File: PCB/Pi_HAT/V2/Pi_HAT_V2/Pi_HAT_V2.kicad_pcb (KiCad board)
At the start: 2 copper layers, 59 x 69.6 mm, 18 parts, among them J1 MPU9250, J2 Pi GPIO, J3 Display, J4 Solenoid I2C, J5 XT60PW-M

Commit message: Still more to do
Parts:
- removed VR1, VR2, VR3: LM78M05CDTX/NOPB, .pretty:VREG_L7805ACD2T
- added C1: 22u, Capacitor_SMD:C_1210_3225Metric_Pad1.33x2.70mm_HandSolder, F.Cu at (65.8, 88.9)
- added C2: 22u, Capacitor_SMD:C_1210_3225Metric_Pad1.33x2.70mm_HandSolder, F.Cu at (65.8, 93.2)
- added C3: 100n, Capacitor_SMD:C_0805_2012Metric_Pad1.18x1.45mm_HandSolder, F.Cu at (59.4, 97.3)
- added C4: 100n, Capacitor_SMD:C_0805_2012Metric_Pad1.18x1.45mm_HandSolder, F.Cu at (54.6, 97.3)
- added C5: 22u, Capacitor_SMD:C_1210_3225Metric_Pad1.33x2.70mm_HandSolder, F.Cu at (71.9, 86.8)
- added C6: 22u, Capacitor_SMD:C_1210_3225Metric_Pad1.33x2.70mm_HandSolder, F.Cu at (72.7, 82.5)
- added C7: 22u, Capacitor_SMD:C_1210_3225Metric_Pad1.33x2.70mm_HandSolder, F.Cu at (66.7, 82.5)
- added L1: 4.7u, .pretty:744777004, F.Cu at (56.9, 91.3)
- added R1: 75K, Resistor_SMD:R_0805_2012Metric_Pad1.20x1.40mm_HandSolder, F.Cu at (65.2, 96.8)
- added R2: 180K, Resistor_SMD:R_1206_3216Metric_Pad1.30x1.75mm_HandSolder, F.Cu at (78.7, 82.0)
- added R3: 20, Resistor_SMD:R_0805_2012Metric_Pad1.20x1.40mm_HandSolder, F.Cu at (77.1, 90.4)
- added R4: 20, Resistor_SMD:R_0805_2012Metric_Pad1.20x1.40mm_HandSolder, F.Cu at (78.1, 85.2)
- added R5: 7.5K, Resistor_SMD:R_0805_2012Metric_Pad1.20x1.40mm_HandSolder, F.Cu at (71.2, 94.8)
- added RV1: 200K, .pretty:TRIM_3296W-1-204LF, F.Cu at (58.1, 83.6)
- added U1: MP2315GJ-Z, .pretty:SOT65P280X100-8N, F.Cu at (72.1, 91.1)
- C1: value C -> 22u; footprint Capacitor_THT:C_Rect_L7.0mm_W2.5mm_P5.00mm -> Capacitor_SMD:C_1210_3225Metric_Pad1.33x2.70mm_HandSolder
- C2: value C_Polarized -> 22u; footprint Capacitor_THT:CP_Radial_D4.0mm_P1.50mm -> Capacitor_SMD:C_1210_3225Metric_Pad1.33x2.70mm_HandSolder
- G***: moved to B.Cu
- J2: value Pi GPIO -> Pi_GPIO
- TB1: value ARDUINO NANO -> ARDUINO_NANO
- moved C2 34.7 mm to (76.2, 103.1)
- moved G*** 30.4 mm to (118.3, 114.8), turned to -90 degrees
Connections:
- C2 pad 1: /5V -> 12V
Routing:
- net /5V: track 125.2 -> 14.1 mm
- net 12V: track 99.9 -> 34.4 mm
- net GND: track 88.5 -> 36.8 mm, vias 6 -> 2
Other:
- board text added: "PI HAT 08/22/22 EASY CONTROLS Designed by: Jacob Romeo"
- board text removed: "PI HAT EASY CONTROLS Designed by: Jacob Romeo"

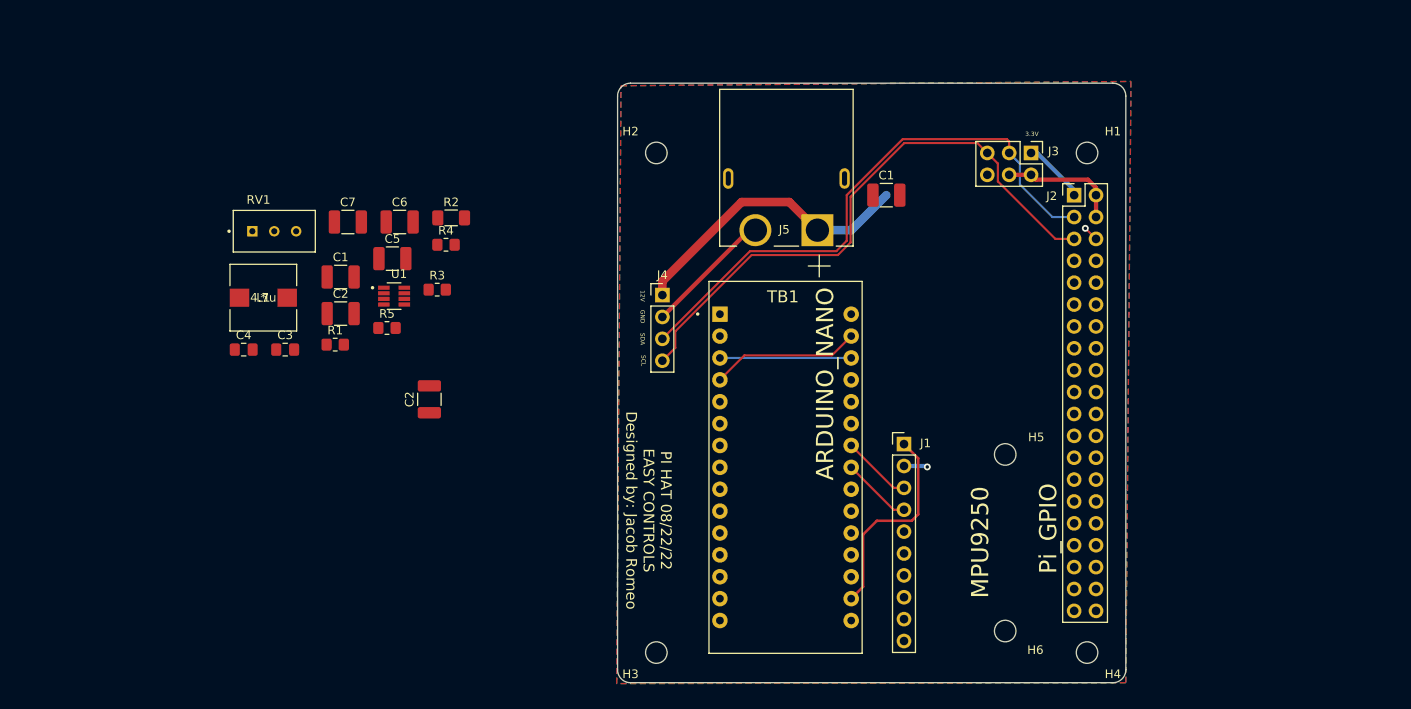
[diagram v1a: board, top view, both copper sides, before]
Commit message: Finished Buch .sch
Next need to start/finish the PCB traces
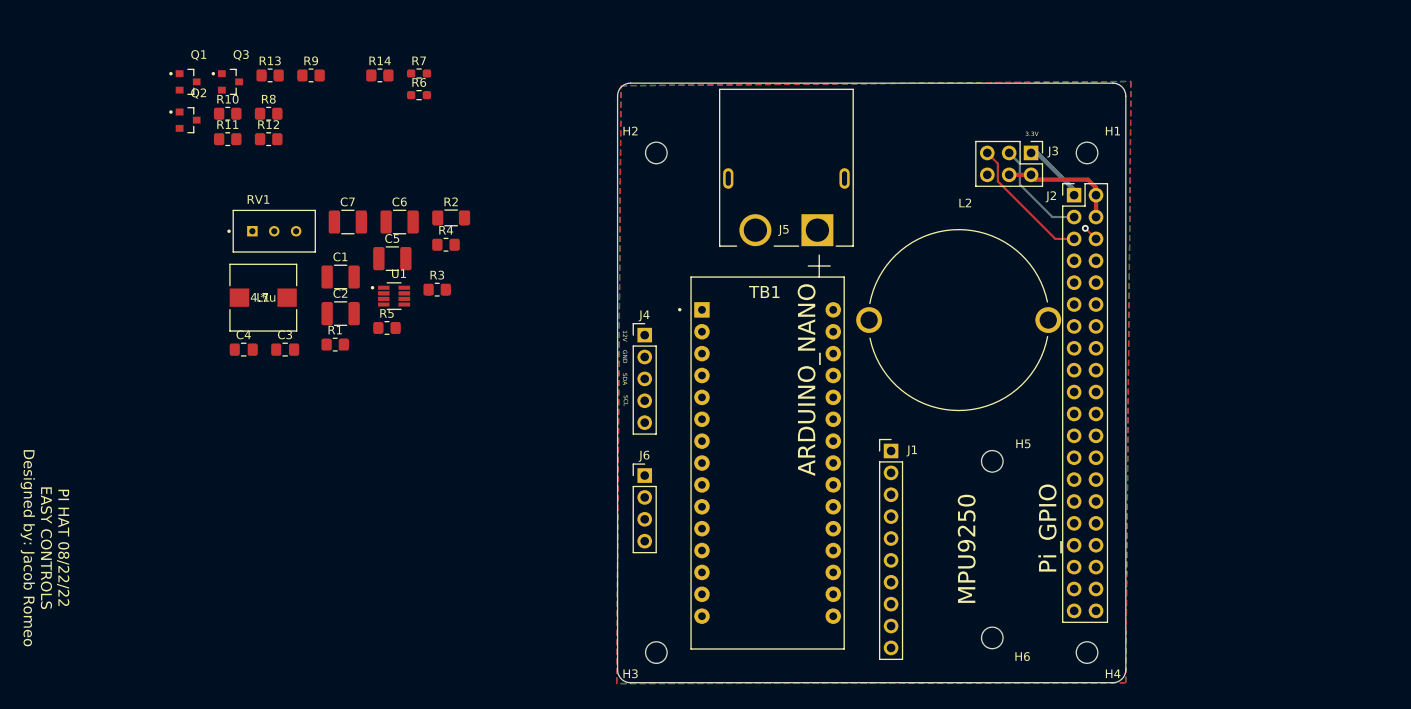
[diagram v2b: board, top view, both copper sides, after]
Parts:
- removed the C1 at (129.2, 79.4)
- removed the C2 at (76.2, 103.1)
- removed G***: LOGO, .pretty:eppl_logo
- added J6: Conn_01x04_Male, Connector_PinHeader_2.54mm:PinHeader_1x04_P2.54mm_Vertical, F.Cu at (101.2, 112.0)
- added L2: 220u, .pretty:IND_AIRD-02-151K, F.Cu at (137.6, 93.9)
- added Q1: BSS138_RFG, .pretty:TRANS_BSS138_RFG, F.Cu at (48.1, 66.2)
- added Q2: BSS138_RFG, .pretty:TRANS_BSS138_RFG, F.Cu at (48.1, 70.7)
- added Q3: BSS138_RFG, .pretty:TRANS_BSS138_RFG, F.Cu at (53.1, 66.2)
- added R10: 10K, Resistor_SMD:R_0805_2012Metric_Pad1.20x1.40mm_HandSolder, F.Cu at (52.7, 70.0)
- added R11: 10K, Resistor_SMD:R_0805_2012Metric_Pad1.20x1.40mm_HandSolder, F.Cu at (52.7, 72.9)
- added R12: 10K, Resistor_SMD:R_0805_2012Metric_Pad1.20x1.40mm_HandSolder, F.Cu at (57.5, 72.9)
- added R13: 10K, Resistor_SMD:R_0805_2012Metric_Pad1.20x1.40mm_HandSolder, F.Cu at (57.7, 65.5)
- added R14: 10K, Resistor_SMD:R_0805_2012Metric_Pad1.20x1.40mm_HandSolder, F.Cu at (70.4, 65.5)
- added R6: 700, Resistor_SMD:R_0603_1608Metric_Pad0.98x0.95mm_HandSolder, F.Cu at (75.0, 67.8)
- added R7: 700, Resistor_SMD:R_0603_1608Metric_Pad0.98x0.95mm_HandSolder, F.Cu at (75.0, 65.3)
- added R8: 10K, Resistor_SMD:R_0805_2012Metric_Pad1.20x1.40mm_HandSolder, F.Cu at (57.5, 70.0)
- added R9: 10K, Resistor_SMD:R_0805_2012Metric_Pad1.20x1.40mm_HandSolder, F.Cu at (62.4, 65.5)
- J4: value Solenoid I2C -> Conn_01x05_Male; footprint Connector_PinHeader_2.54mm:PinHeader_1x04_P2.54mm_Vertical -> Connector_PinHeader_2.54mm:PinHeader_1x05_P2.54mm_Vertical
- moved J4 5.08 mm to (101.2, 95.7)
- moved TB1 2.14 mm to (115.4, 110.5)
- moved H6 1.70 mm to (141.5, 130.8)
- moved H5 1.70 mm to (141.5, 110.3)
- moved J1 1.70 mm to (129.8, 109.1)
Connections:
- J2 pad 10: unconnected-(J2-Pad10) -> /RXP
- J2 pad 8: unconnected-(J2-Pad8) -> /TXP
- J4 pad 3: /SDA -> /SCL
- J4 pad 4: /SCL -> /SDA
- R2 pad 1: unconnected-(R2-Pad1) -> /Buck Converter/SYNC
- TB1 pad 1: unconnected-(TB1-Pad1) -> /TXN
- TB1 pad 2: unconnected-(TB1-Pad2) -> /RXN
- TB1 pad 27: unconnected-(TB1-Pad27) -> /5VN
- TB1 pad 28: unconnected-(TB1-Pad28) -> Net-(R14-Pad2)
- TB1 pad 3: unconnected-(TB1-Pad28) -> Net-(R14-Pad2)
- TB1 pad 30: unconnected-(TB1-Pad30) -> /5V
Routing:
- net /SDA: track 66.4 -> 12.0 mm
- net /SCL: track 68.3 -> 15.4 mm
- net GND: track 36.8 -> 1.75 mm, vias 2 -> 1
- net 12V: track 34.4 -> 0.00 mm
- net 3.3VN: track 24.2 -> 0.00 mm
- net unconnected-(TB1-Pad28): track 15.2 -> 0.00 mm
- net SDAN: track 8.17 -> 0.00 mm
- net SCLN: track 8.17 -> 0.00 mm

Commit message: Updated
Added NANO_HAT and finished the PI_HAT V2 .sch, need to start/finish traces
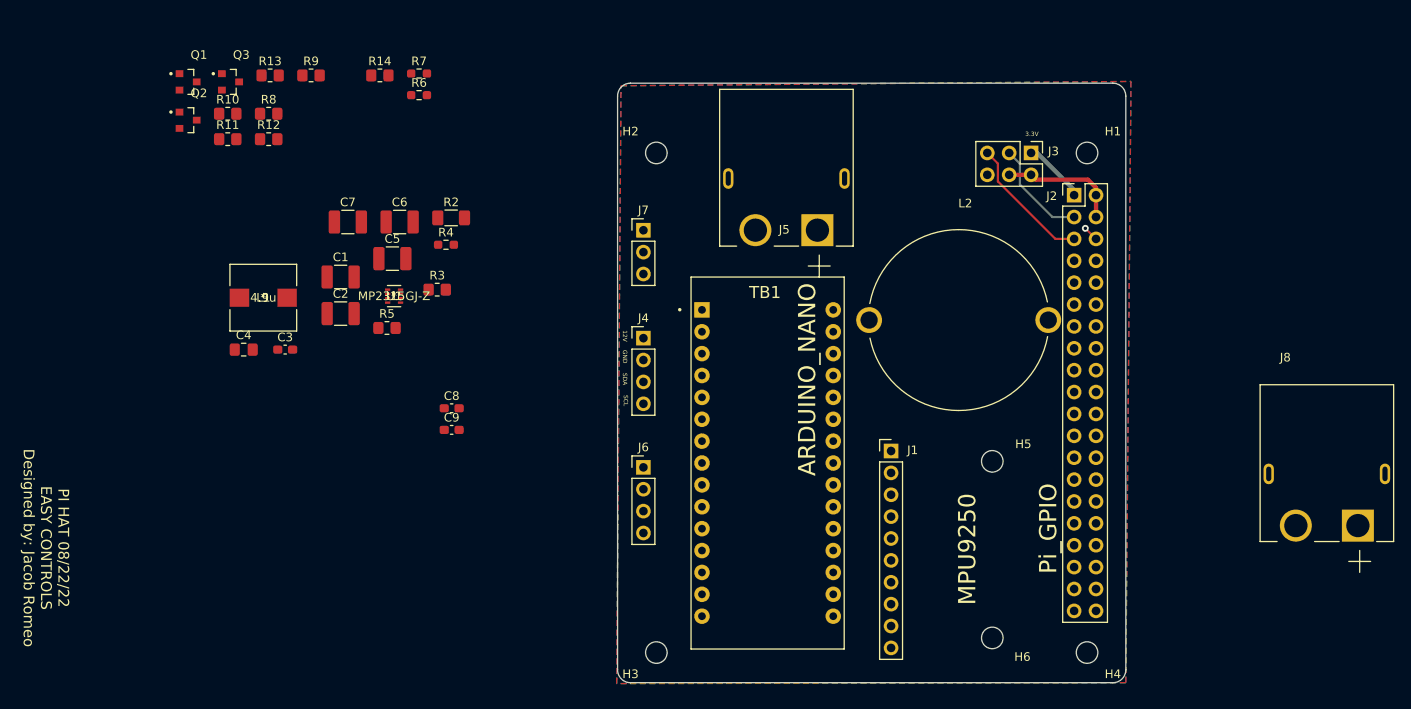
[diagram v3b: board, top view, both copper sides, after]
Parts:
- removed R1: 75K, Resistor_SMD:R_0805_2012Metric_Pad1.20x1.40mm_HandSolder
- removed RV1: 200K, .pretty:TRIM_3296W-1-204LF
- added C8: 6.8n, Capacitor_SMD:C_0603_1608Metric_Pad1.08x0.95mm_HandSolder, F.Cu at (78.7, 104.1)
- added C9: 10p, Capacitor_SMD:C_0603_1608Metric_Pad1.08x0.95mm_HandSolder, F.Cu at (78.7, 106.7)
- added J7: Pressure Sensor, Connector_PinHeader_2.54mm:PinHeader_1x03_P2.54mm_Vertical, F.Cu at (101.0, 83.5)
- added J8: XT60PW-M, .pretty:AMASS_XT60PW-M, F.Cu at (180.3, 111.8)
- C2: value 22u -> 0.1u
- C3: value 100n -> 1n; footprint Capacitor_SMD:C_0805_2012Metric_Pad1.18x1.45mm_HandSolder -> Capacitor_SMD:C_0603_1608Metric_Pad1.08x0.95mm_HandSolder
- C4: value 100n -> 1u
- J4: value Conn_01x05_Male -> Conn_01x04_Male; footprint Connector_PinHeader_2.54mm:PinHeader_1x05_P2.54mm_Vertical -> Connector_PinHeader_2.54mm:PinHeader_1x04_P2.54mm_Vertical
- L1: value 4.7u -> 4.9u
- R14: value 10K -> 40.2k
- R2: value 180K -> 604k
- R3: value 20 -> 15k
- R4: footprint Resistor_SMD:R_0805_2012Metric_Pad1.20x1.40mm_HandSolder -> Resistor_SMD:R_0603_1608Metric_Pad0.98x0.95mm_HandSolder
- R5: value 7.5K -> 7.68K
- U1: footprint .pretty:SOT65P280X100-8N -> .pretty:MP2393GTL-P
- moved J6 0.96 mm to (101.0, 111.0)
- moved J4 0.38 mm to (101.0, 96.0)
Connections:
- R14 pad 1: GND -> Net-(C5-Pad1)
- R14 pad 2: Net-(R14-Pad2) -> Net-(C9-Pad2)
- R2 pad 1: /Buck Converter/SYNC -> 12V
- R3 pad 2: Net-(R3-Pad2) -> Net-(C9-Pad2)
- R5 pad 2: Net-(R3-Pad2) -> Net-(C9-Pad2)
- R6 pad 1: GND -> /SDA
- R6 pad 2: /SDA -> 3.3VP
- R7 pad 1: GND -> /SCL
- R7 pad 2: /SCL -> 3.3VP
- TB1 pad 19: unconnected-(TB1-Pad19) -> /PS
- TB1 pad 28: Net-(R14-Pad2) -> unconnected-(TB1-Pad28)
- TB1 pad 3: Net-(R14-Pad2) -> unconnected-(TB1-Pad28)
- U1 pad 1: Net-(R1-Pad2) -> Net-(C3-Pad1)
- U1 pad 7: Net-(C3-Pad1) -> Net-(C8-Pad1)

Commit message: Updated (Gerber)
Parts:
- removed J8: XT60PW-M, .pretty:AMASS_XT60PW-M
- C1, C2, C3, C4, C5, C6, C7, C8, C9, L1, Q1, Q2, Q3, R10, R11, R12, R13, R14, R2, R3, R4, R5, R6, R7, R8, R9, U1: moved to B.Cu
- moved L1 92.7 mm to (146.5, 67.7)
- moved C4 89.0 mm to (140.2, 73.1), turned to 180 degrees
- moved C3 85.4 mm to (140.2, 69.5), turned to -90 degrees
- moved R7 75.3 mm to (147.8, 84.5), turned to 90 degrees
- moved R6 74.0 mm to (147.8, 80.7), turned to 90 degrees
- moved R5 73.8 mm to (139.2, 66.1), turned to 180 degrees
- moved Q1 70.3 mm to (108.2, 102.7), turned to 90 degrees
- moved C7 70.0 mm to (135.6, 94.9), turned to 180 degrees
- moved Q2 69.5 mm to (113.9, 93.0), turned to -90 degrees
- moved C9 69.4 mm to (135.0, 66.1)
- moved U1 68.7 mm to (137.2, 69.5), turned to 180 degrees
- moved C1 68.0 mm to (132.4, 74.6), turned to 90 degrees
- moved R3 67.7 mm to (139.3, 63.8), turned to 180 degrees
- moved R11 65.4 mm to (113.9, 96.1), turned to 180 degrees
- moved C8 65.0 mm to (133.8, 69.5), turned to -90 degrees
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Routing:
- net /SCL: track 15.4 -> 0.00 mm
- net /SDA: track 12.0 -> 0.00 mm
- net /5V: track 14.1 -> 2.54 mm
- net 3.3VP: track 7.38 -> 0.00 mm
- net GND: track 1.75 -> 0.00 mm, vias 1 -> 0
- removed copper zone on B.Cu, net GND
- removed copper zone on F.Cu, net GND
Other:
- board size 59 x 69.6 mm -> 71.7 x 75.3 mm

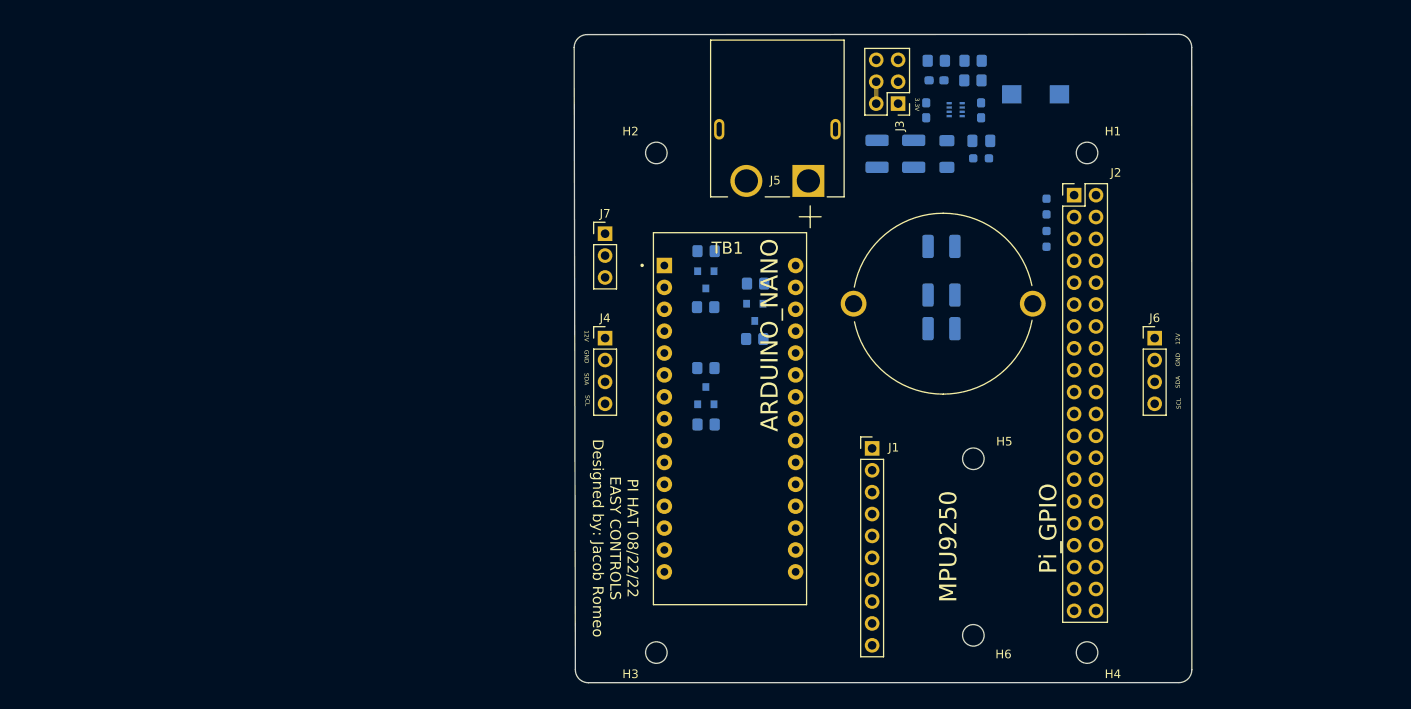
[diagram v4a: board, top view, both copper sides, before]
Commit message: Finished Pi HAT V2
Double checked all 'new' PCB's and made gerbers for all along with a BOM.
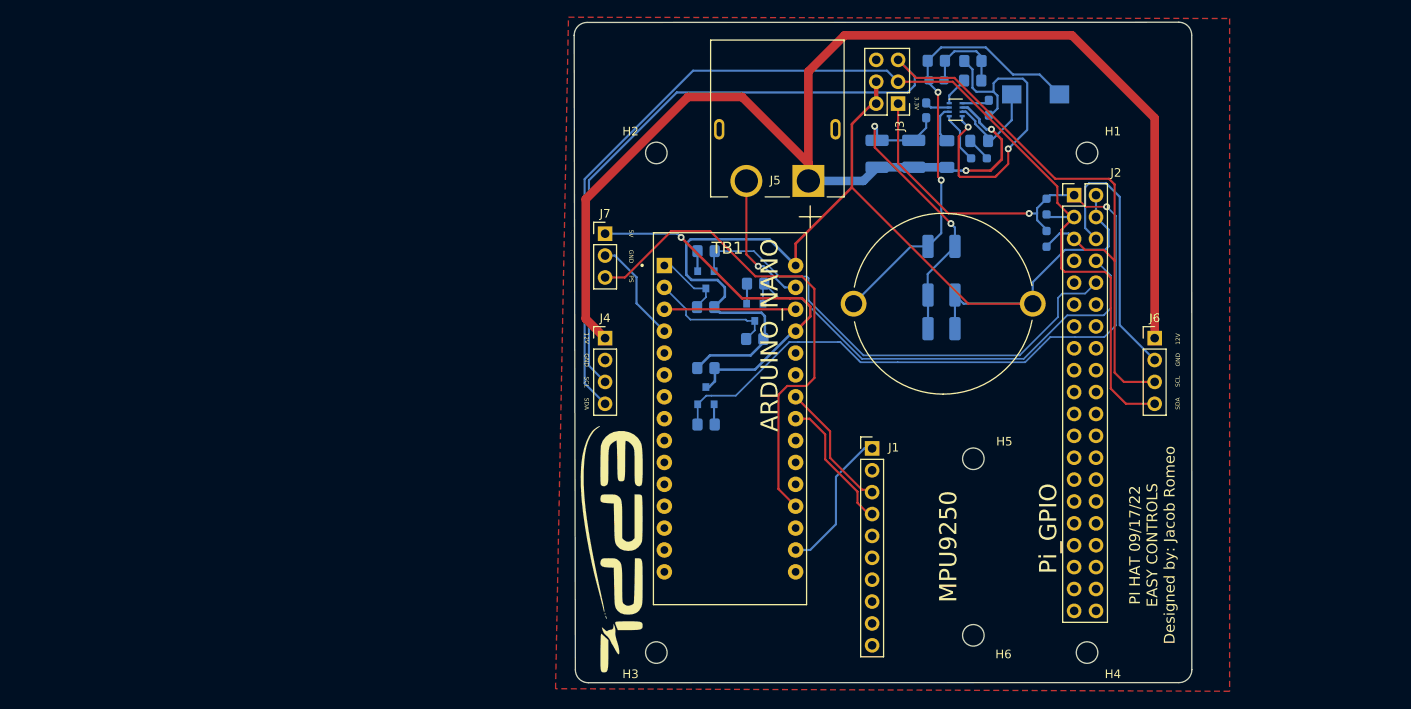
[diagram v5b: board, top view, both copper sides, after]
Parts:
- added G***: LOGO, .pretty:eppl_logo, F.Cu at (97.4, 120.7)
- moved R3 2.30 mm to (139.2, 66.1), turned to 0 degrees
- moved R5 2.25 mm to (139.2, 63.8), turned to 0 degrees
- moved C3 0.95 mm to (141.1, 69.2)
- moved C4 0.25 mm to (140.0, 73.1)
- moved R4 0.25 mm to (139.9, 75.1)
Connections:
- R11 pad 1: VCC -> /5V
- R13 pad 1: VDC -> /5V
- R9 pad 1: +5V -> /5V
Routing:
- net 12V: track 0.00 -> 169.7 mm, vias 0 -> 2
- net /SCL: track 0.00 -> 138.3 mm
- net GND: track 0.00 -> 137.4 mm, vias 0 -> 5
- net /SDA: track 0.00 -> 132.1 mm
- net /5V: track 2.54 -> 129.0 mm
- net 3.3VP: track 0.00 -> 108.7 mm, vias 0 -> 2
- net /PS: track 0.00 -> 58.4 mm
- net /RXP: track 0.00 -> 57.9 mm
- net /TXP: track 0.00 -> 54.9 mm
- net Net-(C5-Pad1): track 0.00 -> 52.4 mm, vias 0 -> 2
- net /5VN: track 0.00 -> 45.1 mm, vias 0 -> 1
- net 3.3VN: track 0.00 -> 17.0 mm
- net SDAN: track 0.00 -> 15.9 mm
- net SCLN: track 0.00 -> 15.3 mm
- net unconnected-(TB1-Pad28): track 0.00 -> 15.2 mm
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- added copper zone on F.Cu, net GND
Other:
- board size 71.7 x 75.3 mm -> 71.7 x 76.7 mm
- board text added: "5V"
- board text added: "PI HAT 09/17/22 EASY CONTROLS Designed by: Jacob Romeo"
- board text added: "PS"
- board text removed: "PI HAT 08/22/22 EASY CONTROLS Designed by: Jacob Romeo"
